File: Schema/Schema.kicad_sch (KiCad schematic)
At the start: 6 parts, among them SW1 SW_Push, U1 ATmega328P-P, Y1 16MHz

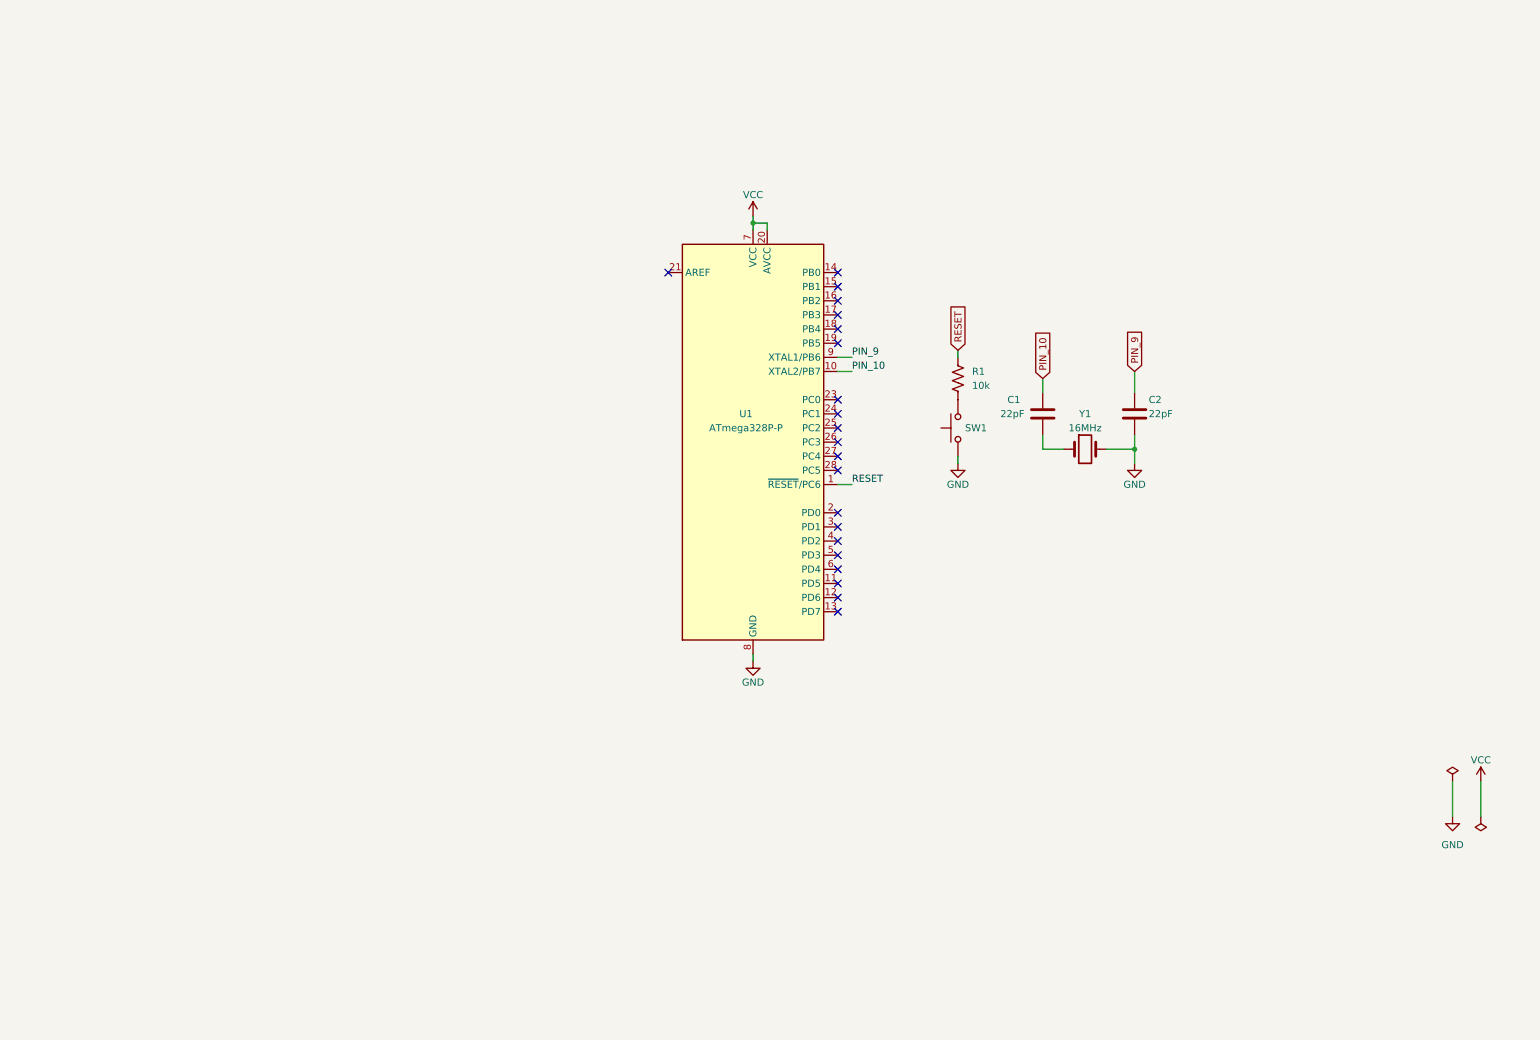
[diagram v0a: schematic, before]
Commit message: Add thermometers to schema
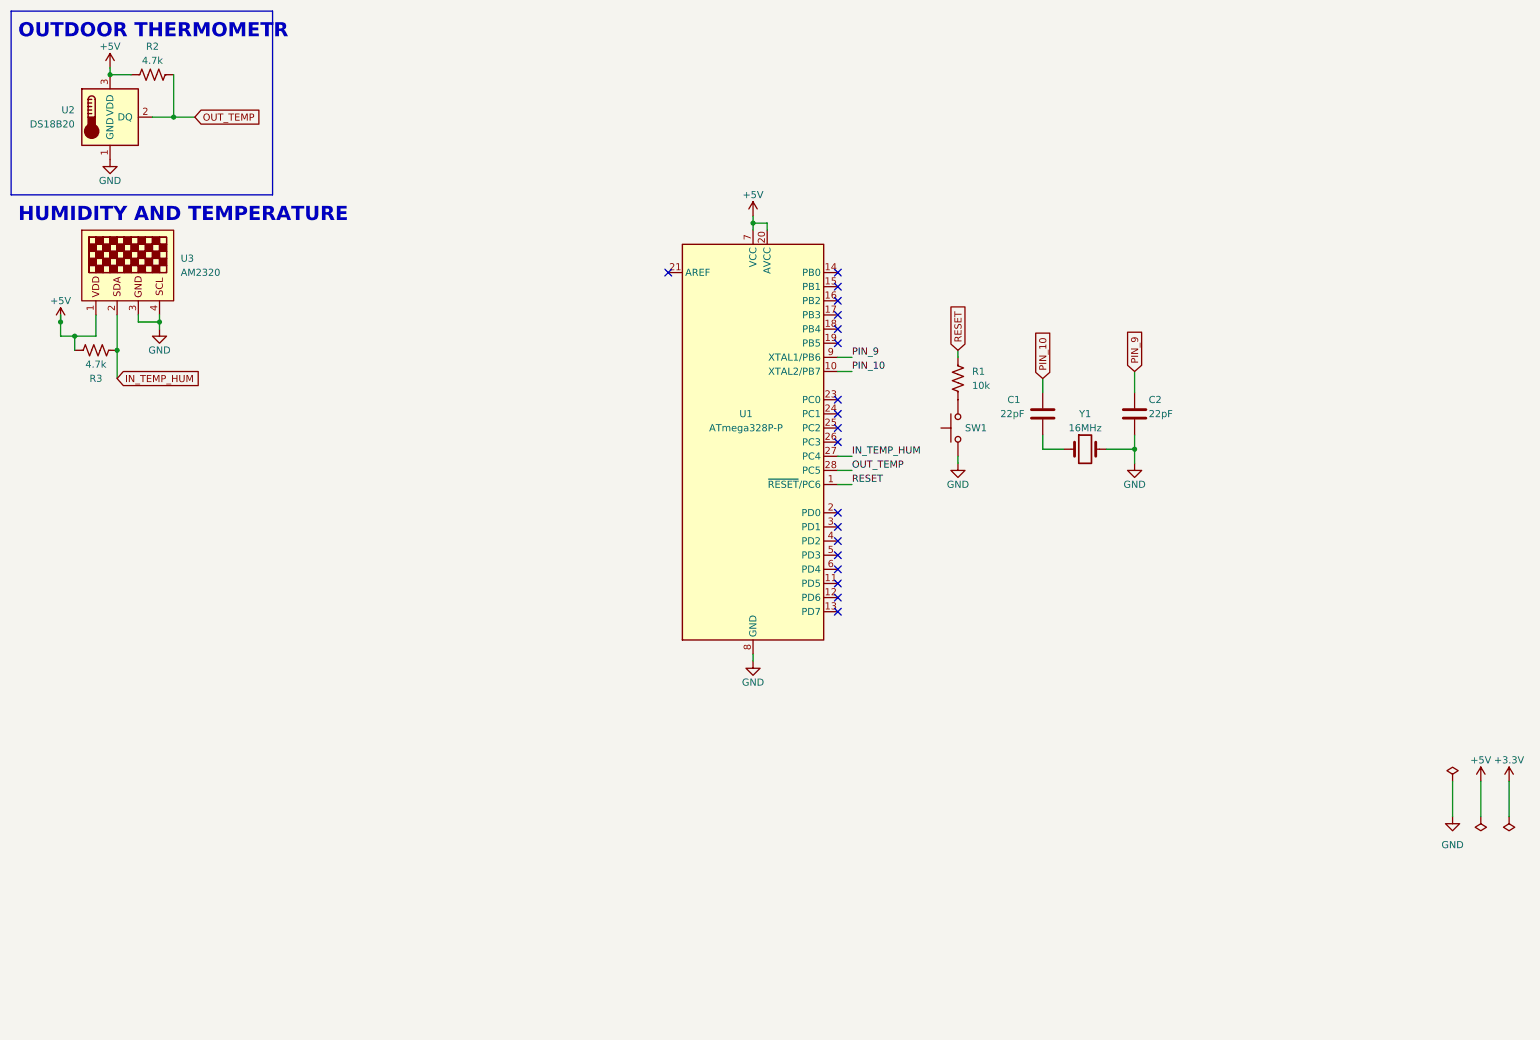
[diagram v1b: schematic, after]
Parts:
- added R2, R3: 4.7k, symbol Device:R_US
- added U2: DS18B20, Package_TO_SOT_THT:TO-92_Inline, symbol Sensor_Temperature:DS18B20
- added U3: AM2320, symbol SM_Library:AM2320
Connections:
- net GND: now also U2.1 (GND), U3.3, U3.4
- net IN_TEMP_HUM: now reaches U1.27 (PC4)
- net IN_TEMP_HUM: now also R3.1, U3.2
- net OUT_TEMP: now reaches U1.28 (PC5)
- net OUT_TEMP: now also R2.2, U2.2 (DQ)
- net VCC renamed +5V
- net +5V: now also R2.1, R3.2, U2.3 (VDD), U3.1
- no-connect marks 21 -> 19
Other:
- note added: "HUMIDITY AND TEMPERATURE"
- note added: "OUTDOOR THERMOMETR"

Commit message: Add all sensors and screen
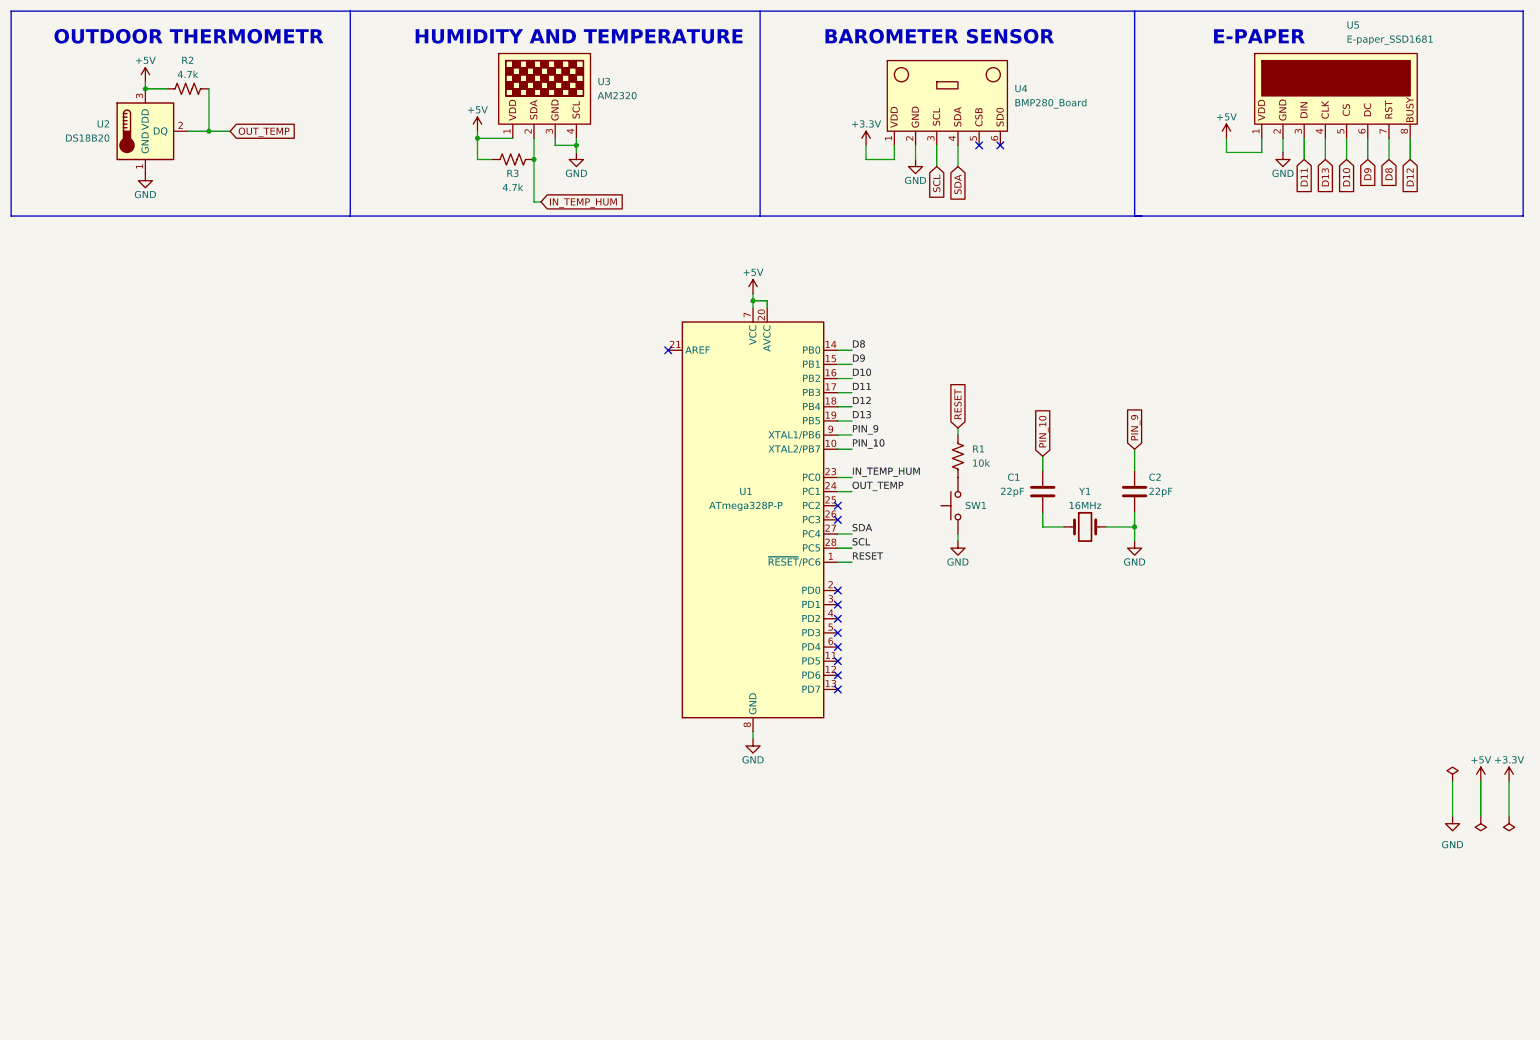
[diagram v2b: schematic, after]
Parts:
- added U4: BMP280_Board, symbol SM_Library:BMP280_Board
- added U5: E-paper_SSD1681, symbol SM_Library:E-paper_SSD1681
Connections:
- net +3.3V: now also U4.1
- net +5V: now also U5.1
- net GND: now also U4.2, U5.2
- net IN_TEMP_HUM: now also U1.23 (PC0); no longer U1.27 (PC4)
- net OUT_TEMP: now also U1.24 (PC1); no longer U1.28 (PC5)
- net D8: now reaches U1.14 (PB0)
- net D8: now also U5.7
- net D9: now reaches U1.15 (PB1)
- net D9: now also U5.6
- net D10: now reaches U1.16 (PB2)
- net D10: now also U5.5
- net D11: now reaches U1.17 (PB3)
- net D11: now also U5.3
- net D12: now reaches U1.18 (PB4)
- net D12: now also U5.8
- net D13: now reaches U1.19 (PB5)
- net D13: now also U5.4
- new net SCL: U1.28 (PC5), U4.3
- new net SDA: U1.27 (PC4), U4.4
- no-connect marks 19 -> 13
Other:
- note added: "BAROMETER SENSOR"
- note added: "E-PAPER"
- moved on the sheet: C1, C2, R1, R2, R3, SW1, U1, U2, U3, Y1

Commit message: Add temporary power ciruit and arrangement of elements
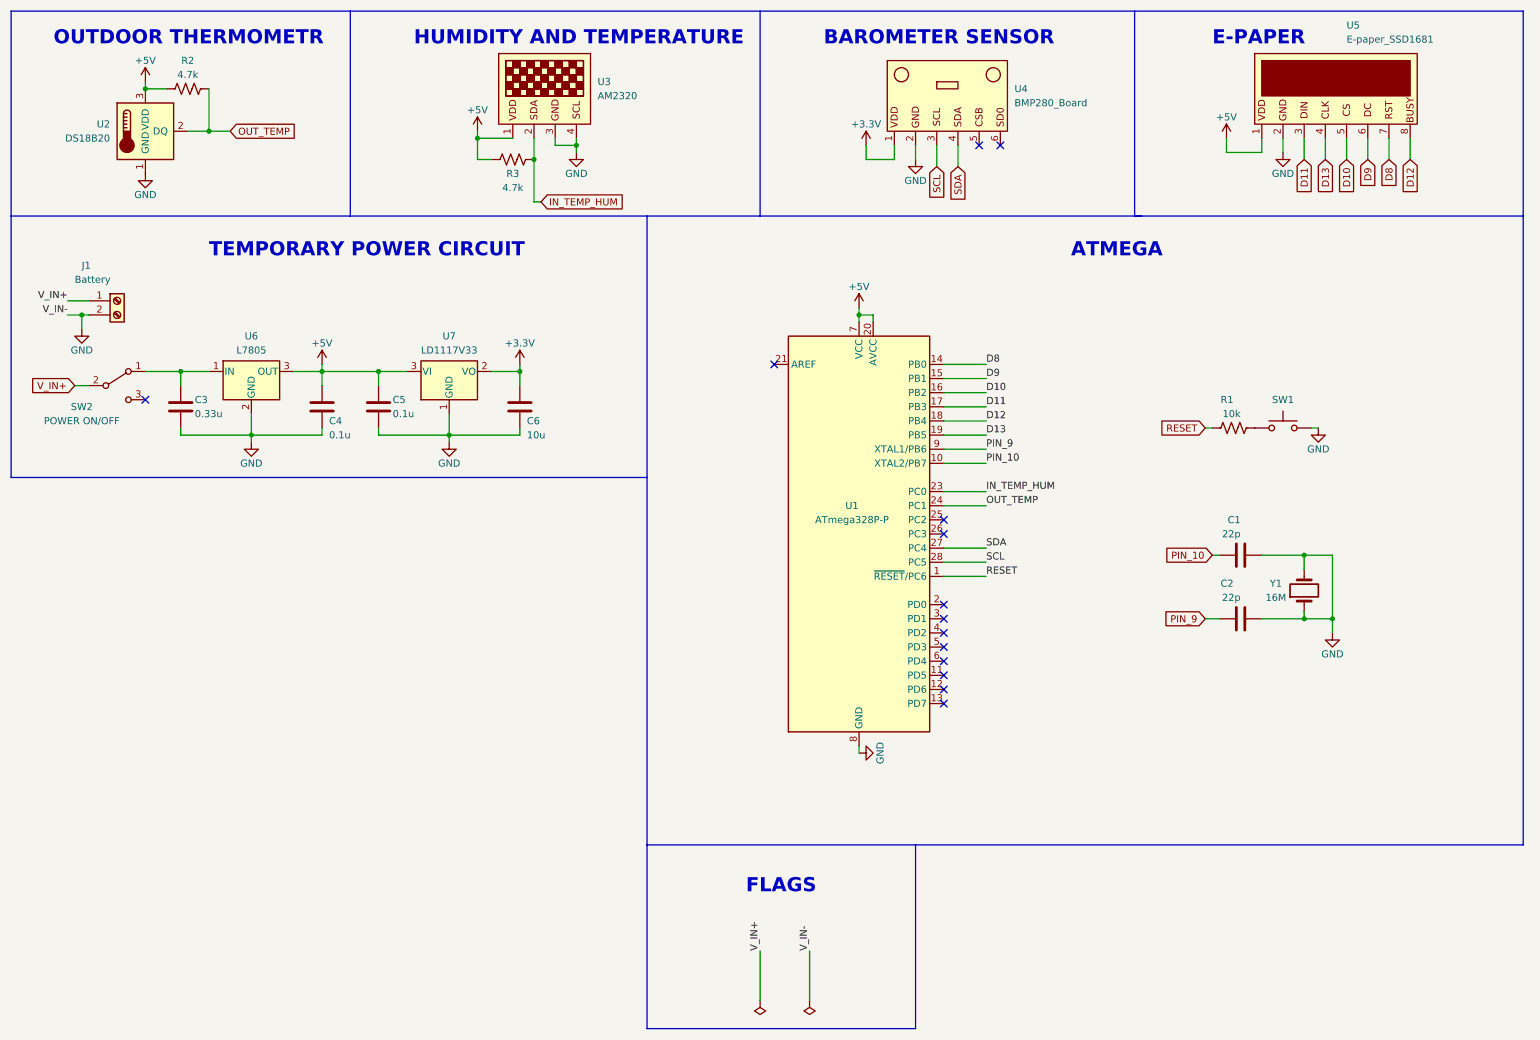
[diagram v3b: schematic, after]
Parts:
- added C3: 0.33u, symbol Device:C
- added C4, C5: 0.1u, symbol Device:C
- added C6: 10u, symbol Device:C
- added J1: Battery, symbol Connector:Screw_Terminal_01x02
- added SW2: POWER ON/OFF, symbol Switch:SW_SPDT
- added U6: L7805, symbol Regulator_Linear:L7805
- added U7: LD1117V33, Package_TO_SOT_SMD:SOT-223-3_TabPin2, symbol Regulator_Linear:LD1117S33TR_SOT223
- C1, C2: value 22pF -> 22p
- Y1: value 16MHz -> 16M
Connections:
- net +3.3V: now also C6.1, U7.2 (VO)
- net +5V: now also C4.1, C5.1, U6.3 (OUT), U7.3 (VI)
- net GND: now also C1.2, SW1.2, Y1.1, C3.2, C4.2, C5.2, C6.2, J1.2 (Pin_2), U6.2 (GND), U7.1 (GND); no longer SW1.1
- net at R1.1: now also SW1.1; no longer SW1.2
- new net: C3.1, SW2.1 (A), U6.1 (IN)
- new net V_IN+: J1.1 (Pin_1), SW2.2 (B)
- no-connect marks 13 -> 14
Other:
- note added: "ATMEGA"
- note added: "FLAGS"
- note added: "TEMPORARY POWER CIRCUIT"
- moved on the sheet: C1, C2, R1, SW1, U1, Y1

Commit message: Add two action buttons
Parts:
- added R4, R5: 10k, symbol Device:R_US
- added SW3, SW4: SW_Push, symbol Switch:SW_Push
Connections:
- net +5V: now also SW3.1, SW4.1
- net GND: now also R4.1, R5.1
- net BT1: now reaches U1.12 (PD6)
- net BT1: now also R4.2, SW3.2
- net BT2: now reaches U1.13 (PD7)
- net BT2: now also R5.2, SW4.2
- no-connect marks 14 -> 12
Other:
- note added: "ACTION BUTTONS"
